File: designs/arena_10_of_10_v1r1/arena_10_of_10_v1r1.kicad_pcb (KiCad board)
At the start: 6 copper layers, 248.9 x 228.6 mm, 519 parts, among them J1 Cetus RJ45 Magjack, J10 Conn_01x05, J11 Conn_01x05, J12 Conn_01x05, J13 Conn_01x05, J14 Conn_01x05, J15 Conn_01x05, J16 Conn_01x05, J17 Conn_01x05, J18 Conn_01x05, J19 Conn_01x05, J2 Conn_01x02, J20 Conn_01x05, J21 Conn_01x05, J22 Conn_01x05, J23 Conn_01x05, J24 Conn_01x05, J25 Barrel_Jack, J26 Barrel_Jack, J27 Conn_Coaxial, J28 Conn_Coaxial, J29 Conn_Coaxial, J3 Conn_Coaxial, J4 Conn_Coaxial, J5 Conn_01x05, J6 Conn_01x05, J7 Conn_01x05, J8 Conn_01x05, J9 Conn_01x05, P1 NA, P10 NA, P2 NA, P3 NA, P4 NA, P5 NA, P6 NA, P7 NA, P8 NA, P9 NA, SW1 SW_SPDT, U1 Teensy4.1, U10 74LVC2G17, U100 74LVC1G125, U101 74LVC2G17, U102 SN74HCS08, U103 SN74HCS08, U104 74LVC1G125, U105 74LVC2G17, U106 SN74HCS08, U107 SN74HCS08, U108 74LVC1G125, U109 74LVC2G17, U11 74LVC2G17, U112 74LVC1G125, U113 74LVC2G17, U116 74LVC1G125, U117 74LVC2G17, U12 74LVC2G17, U120 74LVC1G125, U121 74LVC2G17, U124 74LVC1G125, U125 74LVC2G17, U13 74LVC2G17, U14 74LVC2G17, U15 74LVC2G17, U16 74LVC2G17, U17 74LVC2G17, U18 74LVC2G17, U19 74LVC2G17, U2 SN74LV1T34DBV, U20 74LVC2G17, U21 74LVC2G17, U22 74LVC2G17, U23 74LVC2G17, U24 74LVC2G17, U25 74LVC2G17, U26 74LVC2G17, U27 74LVC2G17, U28 74LVC2G17, U29 74LVC2G17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

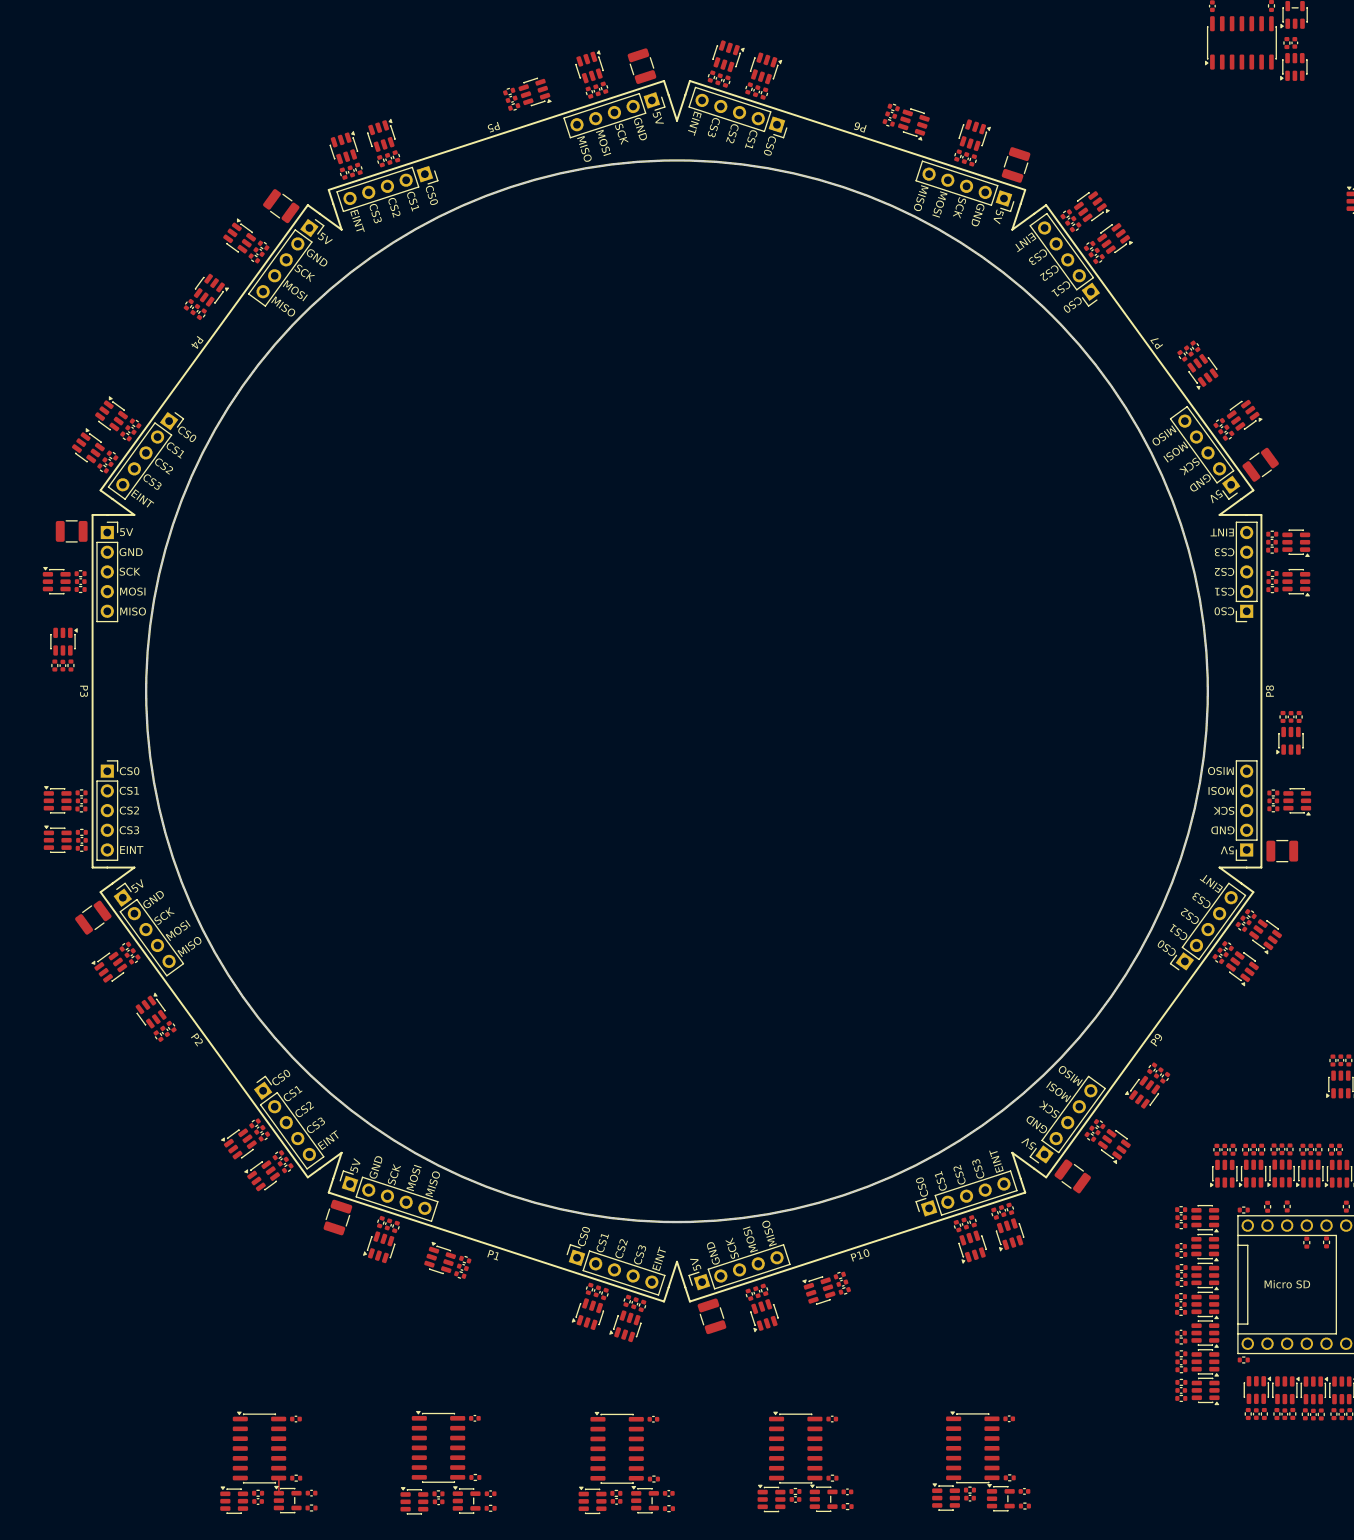
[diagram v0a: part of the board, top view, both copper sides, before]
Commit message: Complete manual route for panel headers.
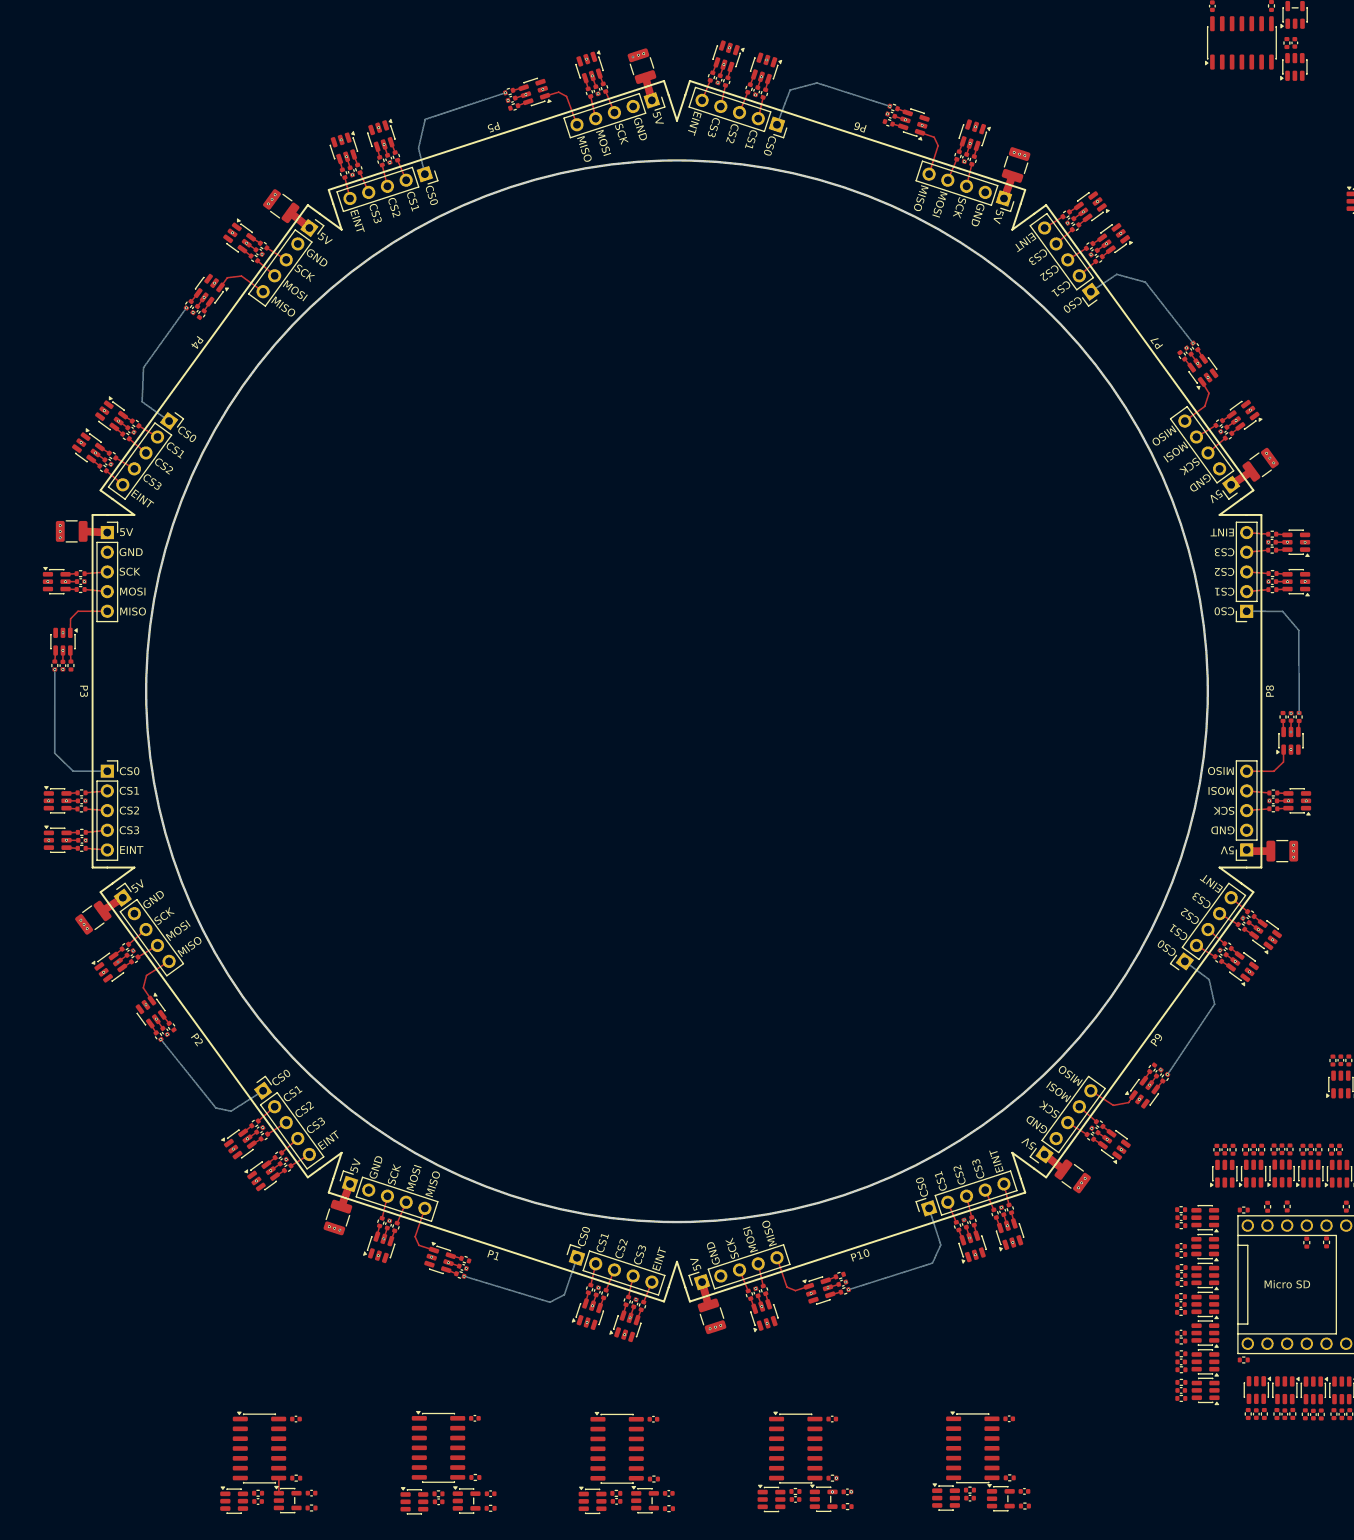
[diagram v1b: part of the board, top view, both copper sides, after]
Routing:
- net +3.3V: track 0.00 -> 59.4 mm, vias 0 -> 42
- net +5V: track 0.00 -> 31.3 mm
- net /Panels/Panel Column P10/Column Buffer/CS0_OUT: track 0.00 -> 18.9 mm, vias 0 -> 1
- net /Panels/Panel Column P1/Column Buffer/CS0_OUT: track 0.00 -> 18.7 mm, vias 0 -> 1
- net /Panels/Panel Column P3/Column Buffer/CS0_OUT: track 0.00 -> 18.5 mm, vias 0 -> 1
- net /Panels/Panel Column P8/Column Buffer/CS0_OUT: track 0.00 -> 18.5 mm, vias 0 -> 1
- net /Panels/Panel Column P2/Column Buffer/CS0_OUT: track 0.00 -> 18.3 mm, vias 0 -> 1
- net /Panels/Panel Column P6/Column Buffer/CS0_OUT: track 0.00 -> 18.3 mm, vias 0 -> 1
- net /Panels/Panel Column P4/Column Buffer/CS0_OUT: track 0.00 -> 18.2 mm, vias 0 -> 1
- net /Panels/Panel Column P5/Column Buffer/CS0_OUT: track 0.00 -> 18.2 mm, vias 0 -> 1
- net /Panels/Panel Column P9/Column Buffer/CS0_OUT: track 0.00 -> 18.1 mm, vias 0 -> 1
- net /Panels/Panel Column P7/Column Buffer/CS0_OUT: track 0.00 -> 17.8 mm, vias 0 -> 1
- net /Panels/Panel Column P1/Column Buffer/MISO_IN: track 0.00 -> 7.12 mm
- net /Panels/Panel Column P2/Column Buffer/MISO_IN: track 0.00 -> 7.07 mm
- net /Panels/Panel Column P10/Column Buffer/MISO_IN: track 0.00 -> 7.02 mm
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
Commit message: Further work on manual route.
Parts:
- moved C27 3.67 mm to (259.9, 271.1)
- moved R70 3.67 mm to (260.9, 271.1)
- moved U27 3.67 mm to (259.9, 268.0)
- moved R71 3.67 mm to (258.9, 271.1)
- moved C28 3.66 mm to (256.3, 271.1)
- moved U28 3.66 mm to (256.3, 268.0)
- moved R73 3.66 mm to (255.2, 271.1)
- moved R72 3.66 mm to (257.3, 271.1)
- moved R22 0.84 mm to (300.3, 259.7)
- moved R21 0.82 mm to (303.0, 259.7)
- moved R24 0.63 mm to (277.4, 259.8)
- moved R5 0.55 mm to (294.6, 249.3)
- moved R6 0.53 mm to (292.1, 249.3)
- moved R8 0.52 mm to (287.0, 249.3)
- moved R4 0.51 mm to (297.2, 249.3)
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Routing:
- net /Teensy/ETH_R-: track 0.00 -> 39.7 mm
- net +3.3V: track 59.4 -> 98.0 mm, vias 42 -> 69
- net /Teensy/ETH_R+: track 0.00 -> 36.2 mm
- net /Fan Out/TNY.EINT: track 0.00 -> 31.9 mm
- net /Power/SW_5V: track 0.00 -> 30.7 mm
- net /Teensy/ETH_T-: track 0.00 -> 27.9 mm
- net /Teensy/ETH_T+: track 0.00 -> 25.7 mm
- net /Fan Out/TNY.CS_11: track 0.00 -> 25.1 mm
- net /Fan Out/TNY.CS_12: track 0.00 -> 23.2 mm
- net /Fan Out/TNY.CS_13: track 0.00 -> 22.3 mm
- net GND: track 0.92 -> 14.5 mm, vias 111 -> 165
- net /Fan Out/TNY.CS_16: track 0.00 -> 6.08 mm
- net Net-(R187-Pad2): track 0.00 -> 3.88 mm
- net Net-(R193-Pad2): track 0.00 -> 3.75 mm
- net Net-(R214-Pad2): track 0.00 -> 3.55 mm
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
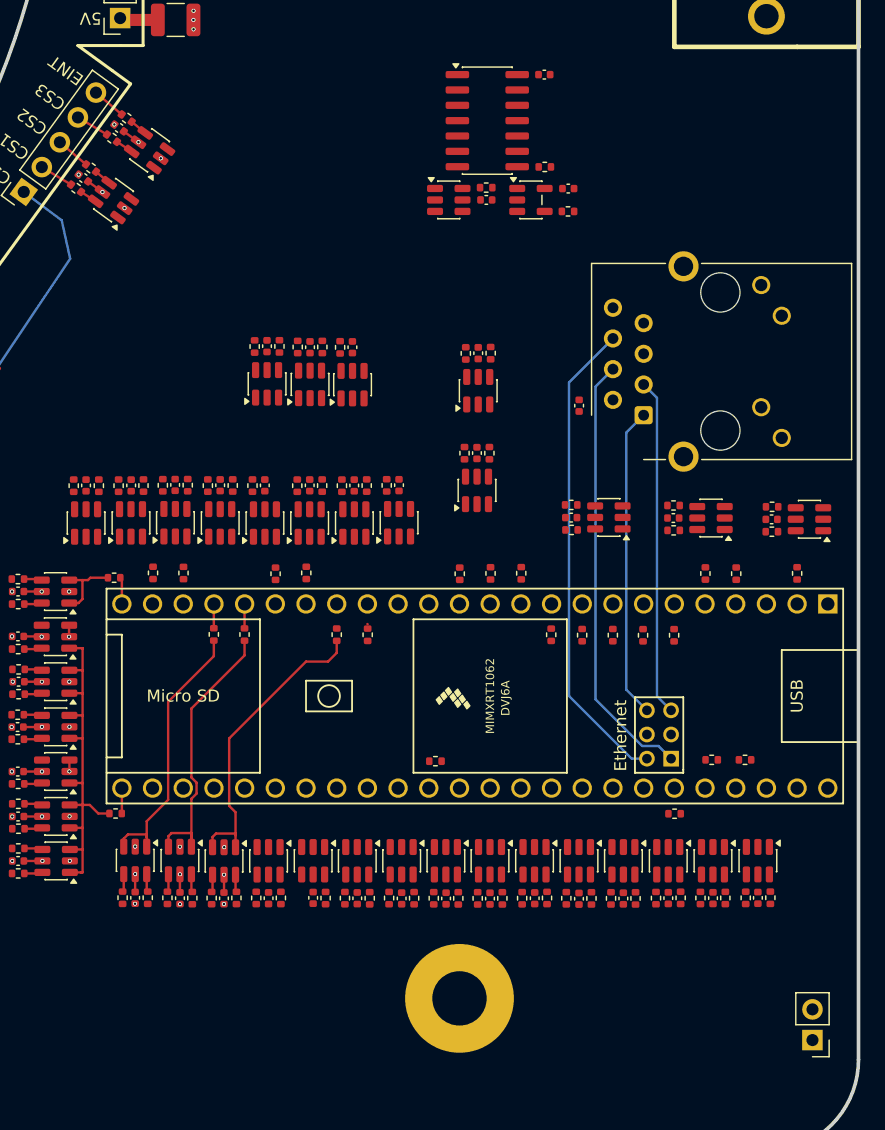
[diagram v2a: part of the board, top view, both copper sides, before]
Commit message: Worked on hand/manual routing - pwr, gnd, special signals, etc.
Finished hand/manual routing around teensy and bottom half of the
PCB. Still need to finish the right hand side.
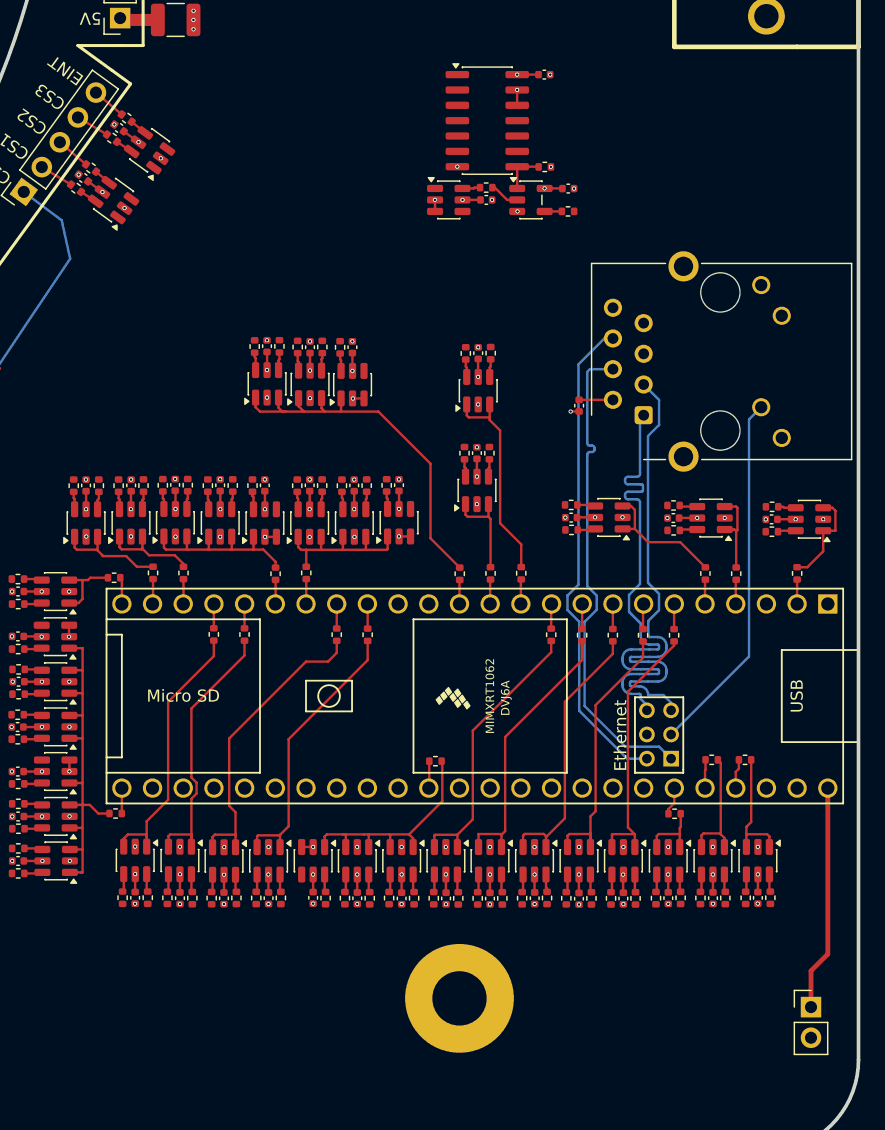
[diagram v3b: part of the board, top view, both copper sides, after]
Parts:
- moved J2 2.73 mm to (308.5, 280.1), turned to 0 degrees
- turned R8 to 90 degrees
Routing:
- net +3.3V: track 98.0 -> 144.8 mm, vias 69 -> 101
- net /Fan Out/TNY.MOSI_B0: track 0.00 -> 32.0 mm
- net /Teensy/ETH_LED: track 0.00 -> 30.2 mm
- net /Fan Out/TNY.CS_07: track 0.00 -> 23.2 mm
- net /Fan Out/TNY.CS_10: track 0.00 -> 22.9 mm
- net /Fan Out/TNY.CS_06: track 0.00 -> 22.8 mm
- net /Fan Out/TNY.CS_05: track 0.00 -> 22.4 mm
- net /Fan Out/TNY.CS_04: track 0.00 -> 22.1 mm
- net /Fan Out/TNY.CS_03: track 0.00 -> 21.8 mm
- net /Fan Out/TNY.SCK_B0: track 0.00 -> 19.5 mm
- net /Teensy/VIN: track 0.00 -> 18.7 mm
- net /Fan Out/TNY.CS_08: track 0.00 -> 17.4 mm
- net /Fan Out/TNY.SCK_B1: track 0.00 -> 15.4 mm
- net /Teensy/ETH_T+: track 25.7 -> 40.4 mm
- net /Fan Out/TNY.MOSI_B1: track 0.00 -> 14.1 mm
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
